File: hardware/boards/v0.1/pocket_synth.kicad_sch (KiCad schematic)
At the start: 7 parts

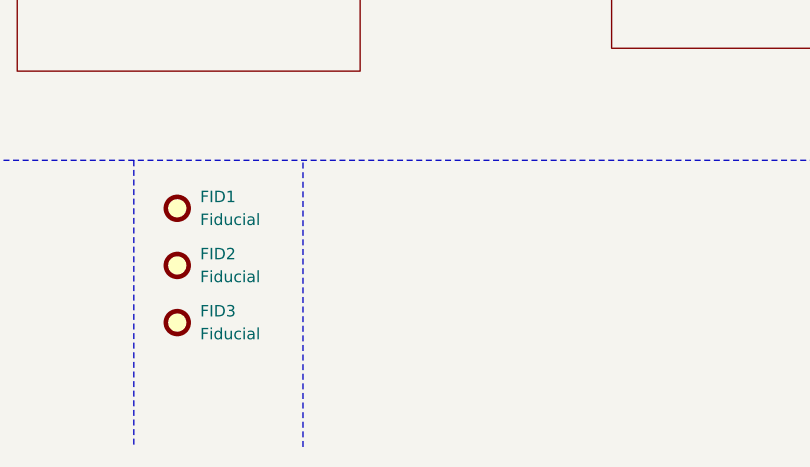
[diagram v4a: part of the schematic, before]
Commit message: feat: route thermalcouple, add top side fiducials
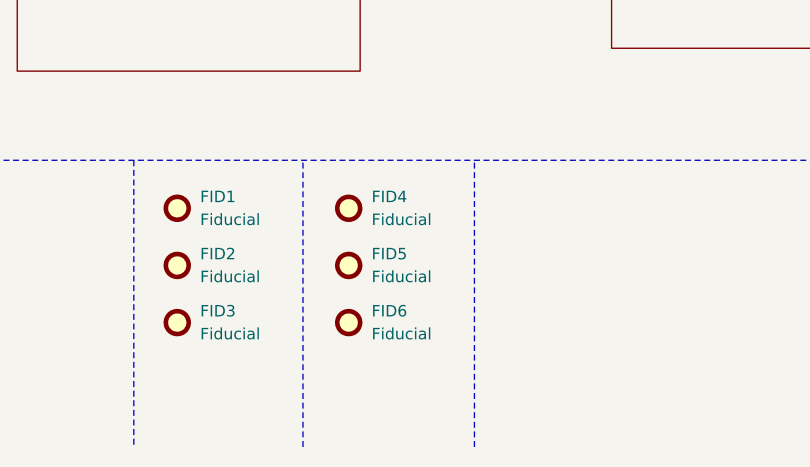
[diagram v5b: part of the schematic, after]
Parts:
- added FID4, FID5, FID6: Fiducial, Fiducial:Fiducial_0.5mm_Mask1.5mm, symbol Mechanical:Fiducial
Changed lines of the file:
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@@
+		)
+	)
+	(polyline
+		(pts
+			(xy 123.19 166.37) (xy 123.19 198.12)
+		)
+		(stroke
+			(width 0.127)
+			(type dash)
 		)
 	)
@@
 	)
 	(symbol
+		(lib_id "Mechanical:Fiducial")
+		(at 109.22 177.8 0)
+		(unit 1)
+		(exclude_from_sim no)
+		(in_bom no)
+		(on_board yes)
+		(dnp no)
+		(fields_autoplaced yes)
+		(property "Reference" "FID5"
+			(at 111.76 176.5299 0)
+			(effects
+				(font
+					(size 1.27 1.27)
+				)
+				(justify left)
+			)
+		)
+		(property "Value" "Fiducial"
+			(at 111.76 179.0699 0)
+			(effects
+				(font
+					(size 1.27 1.27)
+				)
+				(justify left)
+			)
+		)
+		(property "Footprint" "Fiducial:Fiducial_0.5mm_Mask1.5mm"
+			(at 109.22 177.8 0)
+			(effects
+				(font
+					(size 1.27 1.27)
+				)
+				(hide yes)
+			)
+		)
+		(property "Datasheet" "~"
+			(at 109.22 177.8 0)
+			(effects
+				(font
+					(size 1.27 1.27)
+				)
+				(hide yes)
+			)
+		)
+		(property "Description" "Fiducial Marker"
+			(at 109.22 177.8 0)
+			(effects
+				(font
+					(size 1.27 1.27)
+				)
+				(hide yes)
+			)
+		)
+		(instances
+			(project "pocket_synth"
+				(path "/485383b8-00f4-4405-b270-de249939cff4"
+					(reference "FID5")
+					(unit 1)
+				)
+			)
+		)
+	)
+	(symbol
 		(lib_id "Mechanical:MountingHole_Pad")
 		(at 48.26 182.88 0)
@@
 	(symbol
 		(lib_id "Mechanical:Fiducial")
+		(at 109.22 184.15 0)
+		(unit 1)
+		(exclude_from_sim no)
+		(in_bom no)
+		(on_board yes)
+		(dnp no)
+		(fields_autoplaced yes)
+		(property "Reference" "FID6"
+			(at 111.76 182.8799 0)
+			(effects
+				(font
+					(size 1.27 1.27)
+				)
+				(justify left)
+			)
+		)
+		(property "Value" "Fiducial"
+			(at 111.76 185.4199 0)
+			(effects
+				(font
+					(size 1.27 1.27)
+				)
+				(justify left)
+			)
+		)
+		(property "Footprint" "Fiducial:Fiducial_0.5mm_Mask1.5mm"
+			(at 109.22 184.15 0)
+			(effects
+				(font
+					(size 1.27 1.27)
+				)
+				(hide yes)
+			)
+		)
+		(property "Datasheet" "~"
+			(at 109.22 184.15 0)
+			(effects
+				(font
+					(size 1.27 1.27)
+				)
+				(hide yes)
+			)
+		)
+		(property "Description" "Fiducial Marker"
+			(at 109.22 184.15 0)
+			(effects
+				(font
+					(size 1.27 1.27)
+				)
+				(hide yes)
+			)
+		)
+		(instances
+			(project "pocket_synth"
+				(path "/485383b8-00f4-4405-b270-de249939cff4"
+					(reference "FID6")
+					(unit 1)
+				)
+			)
+		)
+	)
+	(symbol
+		(lib_id "Mechanical:Fiducial")
 		(at 90.17 184.15 0)
 		(unit 1)
@@
 					(unit 1)
 				)
+			)
+		)
+	)
+	(symbol
+		(lib_id "Mechanical:Fiducial")
+		(at 109.22 171.45 0)
+		(unit 1)
+		(exclude_from_sim no)
+		(in_bom no)
+		(on_board yes)
+		(dnp no)
+		(fields_autoplaced yes)
+		(property "Reference" "FID4"
+			(at 111.76 170.1799 0)
+			(effects
+				(font
+					(size 1.27 1.27)
+				)
+				(justify left)
+			)
+		)
+		(property "Value" "Fiducial"
+			(at 111.76 172.7199 0)
+			(effects
+				(font
+					(size 1.27 1.27)
+				)
+				(justify left)
+			)
+		)
+		(property "Footprint" "Fiducial:Fiducial_0.5mm_Mask1.5mm"
+			(at 109.22 171.45 0)
+			(effects
+				(font
+					(size 1.27 1.27)
+				)
+				(hide yes)
+			)
+		)
+		(property "Datasheet" "~"
+			(at 109.22 171.45 0)
+			(effects
+				(font
+					(size 1.27 1.27)
+				)
+				(hide yes)
+			)
+		)
+		(property "Description" "Fiducial Marker"
+			(at 109.22 171.45 0)
+			(effects
+				(font
+					(size 1.27 1.27)
+				)
+				(hide yes)
+			)
+		)
+		(instances
+			(project "pocket_synth"
+				(path "/485383b8-00f4-4405-b270-de249939cff4"
+					(reference "FID4")
+					(unit 1)
+				)

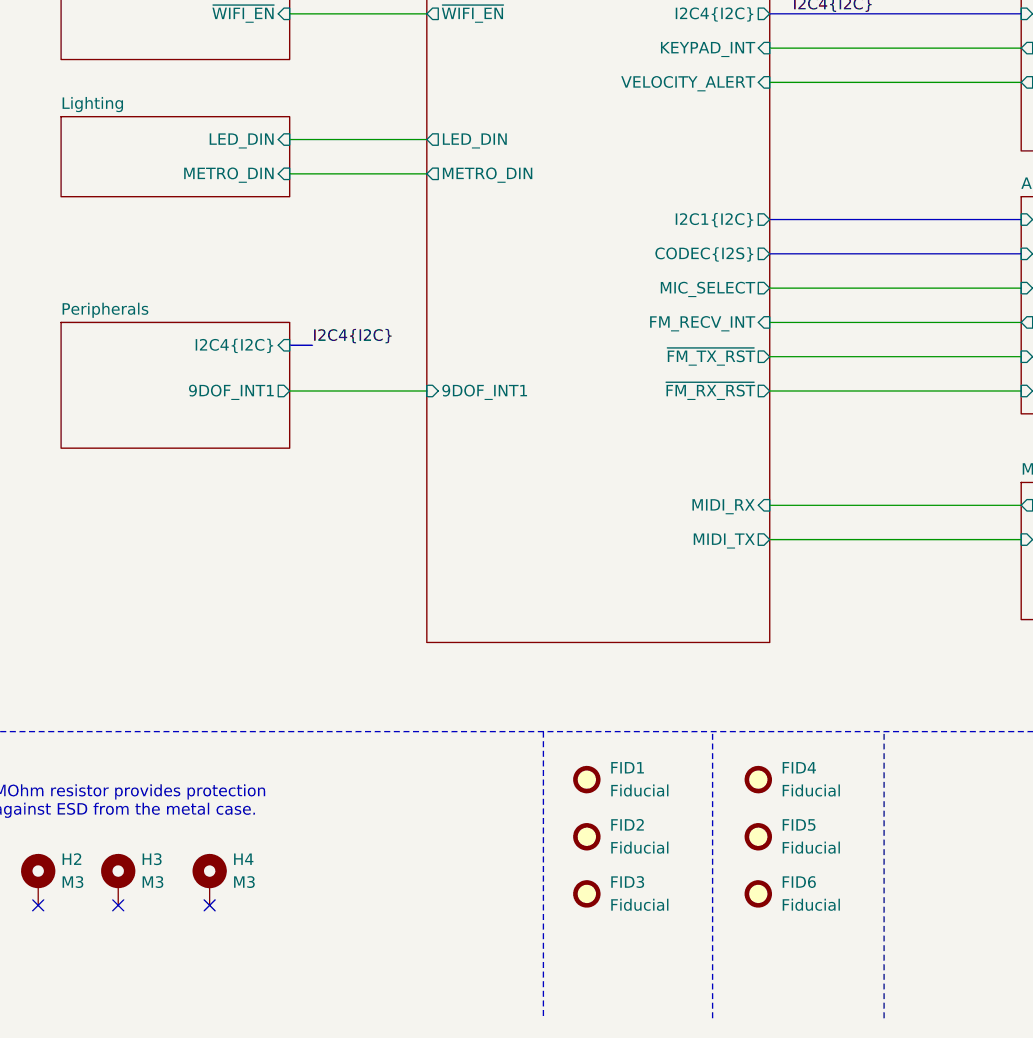
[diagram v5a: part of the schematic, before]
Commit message: feat: clean up routing, remove metronome light
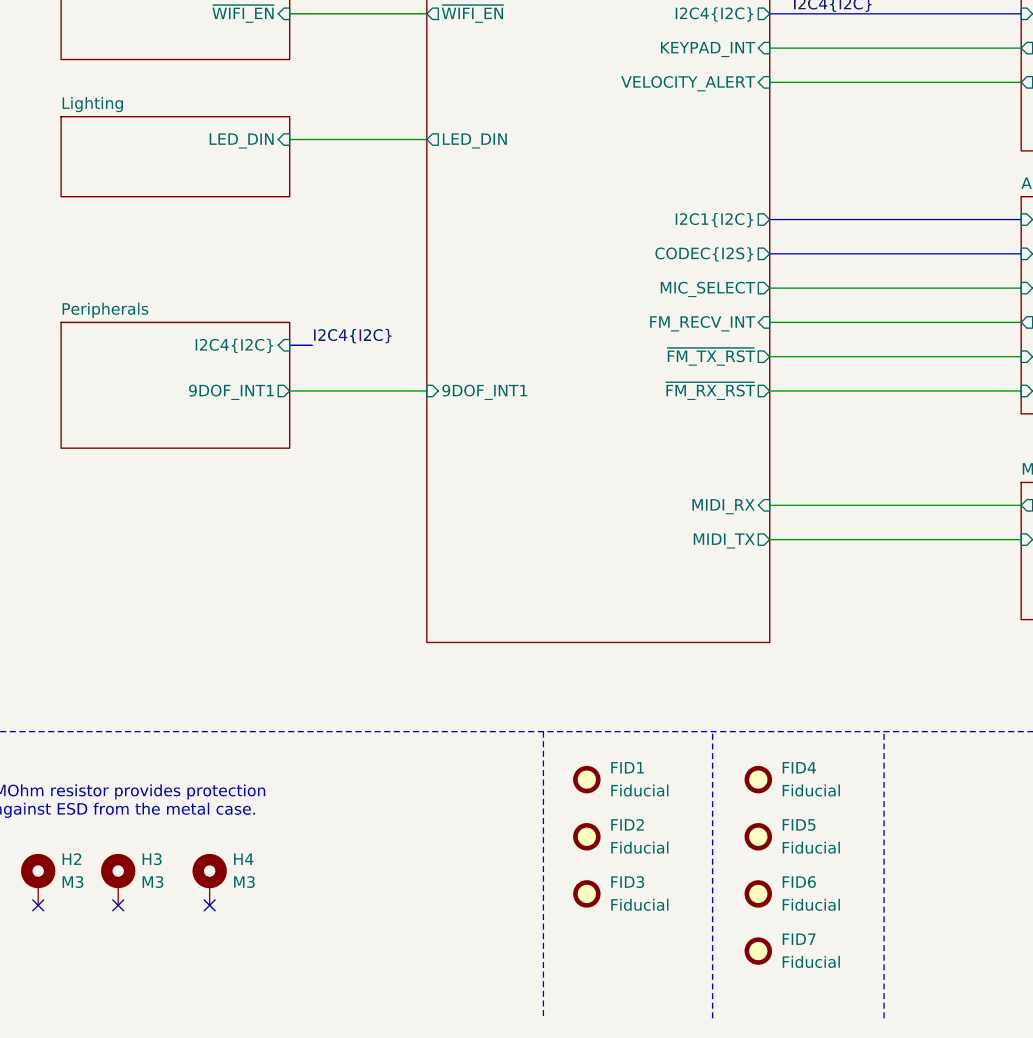
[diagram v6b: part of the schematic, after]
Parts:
- added FID7: Fiducial, Fiducial:Fiducial_0.5mm_Mask1.5mm, symbol Mechanical:Fiducial
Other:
- sheet Lighting ports: added none; removed METRO_DIN
- sheet MCU ports: added none; removed METRO_DIN
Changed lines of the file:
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@@
-	(wire
-		(pts
-			(xy 57.15 104.14) (xy 72.39 104.14)
-		)
-		(stroke
-			(width 0)
-			(type default)
-		)
-	)
 	(wire
 		(pts
@@
 	(symbol
 		(lib_id "Mechanical:Fiducial")
+		(at 109.22 190.5 0)
+		(unit 1)
+		(exclude_from_sim no)
+		(in_bom no)
+		(on_board yes)
+		(dnp no)
+		(fields_autoplaced yes)
+		(property "Reference" "FID7"
+			(at 111.76 189.2299 0)
+			(effects
+				(font
+					(size 1.27 1.27)
+				)
+				(justify left)
+			)
+		)
+		(property "Value" "Fiducial"
+			(at 111.76 191.7699 0)
+			(effects
+				(font
+					(size 1.27 1.27)
+				)
+				(justify left)
+			)
+		)
+		(property "Footprint" "Fiducial:Fiducial_0.5mm_Mask1.5mm"
+			(at 109.22 190.5 0)
+			(effects
+				(font
+					(size 1.27 1.27)
+				)
+				(hide yes)
+			)
+		)
+		(property "Datasheet" "~"
+			(at 109.22 190.5 0)
+			(effects
+				(font
+					(size 1.27 1.27)
+				)
+				(hide yes)
+			)
+		)
+		(property "Description" "Fiducial Marker"
+			(at 109.22 190.5 0)
+			(effects
+				(font
+					(size 1.27 1.27)
+				)
+				(hide yes)
+			)
+		)
+		(instances
+			(project "pocket_synth"
+				(path "/485383b8-00f4-4405-b270-de249939cff4"
+					(reference "FID7")
+					(unit 1)
+				)
+			)
+		)
+	)
+	(symbol
+		(lib_id "Mechanical:Fiducial")
 		(at 90.17 177.8 0)
 		(unit 1)
@@
 			)
 		)
-		(pin "METRO_DIN" output
-			(at 72.39 104.14 180)
-			(effects
-				(font
-					(size 1.27 1.27)
-				)
-				(justify left)
-			)
-		)
 		(pin "VELOCITY_ALERT" input
 			(at 110.49 93.98 0)
@@
 			(effects
 				(font
-					(size 1.27 1.27)
-				)
-				(justify right)
-			)
-		)
-		(pin "METRO_DIN" input
-			(at 57.15 104.14 0)
-			(effects
-				(font

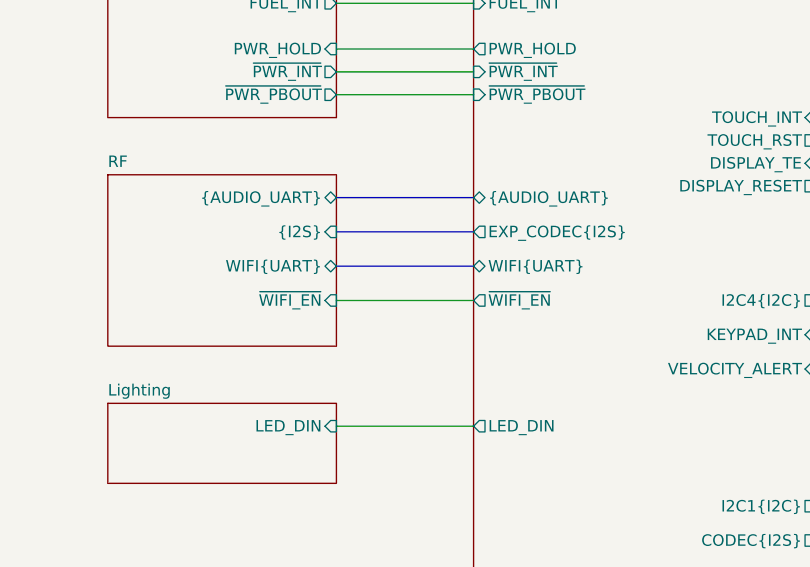
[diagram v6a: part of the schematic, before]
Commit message: feat: routing cleanup and start of BOM selection
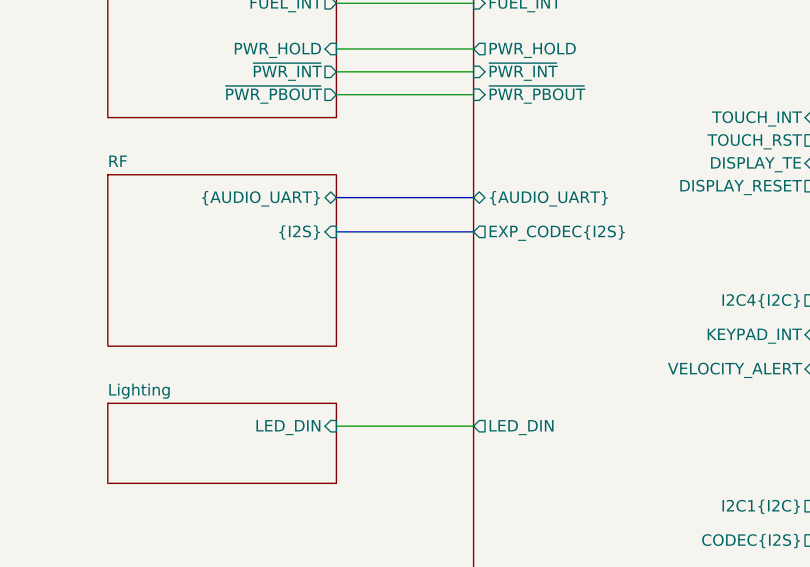
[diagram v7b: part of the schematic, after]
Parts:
- FID1, FID2, FID3, FID4, FID5, FID6, FID7: footprint Fiducial:Fiducial_0.5mm_Mask1.5mm -> PCM_kikit:Fiducial; now in the parts list
- H1, H2, H3, H4: now in the parts list
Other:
- sheet MCU ports: added none; removed WIFI{UART}, ~{WIFI_EN}
- sheet RF ports: added none; removed WIFI{UART}, ~{WIFI_EN}
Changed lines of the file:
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@@
-		)
-	)
-	(bus
-		(pts
-			(xy 57.15 82.55) (xy 72.39 82.55)
-		)
-		(stroke
-			(width 0)
-			(type default)
 		)
 	)
@@
 		(pts
 			(xy 110.49 86.36) (xy 138.43 86.36)
-		)
-		(stroke
-			(width 0)
-			(type default)
-		)
-	)
-	(wire
-		(pts
-			(xy 57.15 86.36) (xy 72.39 86.36)
 		)
 		(stroke
@@
 		(unit 1)
 		(exclude_from_sim no)
-		(in_bom no)
+		(in_bom yes)
 		(on_board yes)
 		(dnp no)
@@
 		(unit 1)
 		(exclude_from_sim no)
-		(in_bom no)
+		(in_bom yes)
 		(on_board yes)
 		(dnp no)
@@
 			)
 		)
-		(property "Footprint" "Fiducial:Fiducial_0.5mm_Mask1.5mm"
+		(property "Footprint" "PCM_kikit:Fiducial"
 			(at 109.22 177.8 0)
 			(effects
@@
 		(unit 1)
 		(exclude_from_sim no)
-		(in_bom no)
+		(in_bom yes)
 		(on_board yes)
 		(dnp no)
@@
 		(unit 1)
 		(exclude_from_sim no)
-		(in_bom no)
+		(in_bom yes)
 		(on_board yes)
 		(dnp no)
@@
 		(unit 1)
 		(exclude_from_sim no)
-		(in_bom no)
+		(in_bom yes)
 		(on_board yes)
 		(dnp no)
@@
 		(unit 1)
 		(exclude_from_sim no)
-		(in_bom no)
+		(in_bom yes)
 		(on_board yes)
 		(dnp no)
@@
 			)
 		)
-		(property "Footprint" "Fiducial:Fiducial_0.5mm_Mask1.5mm"
+		(property "Footprint" "PCM_kikit:Fiducial"
 			(at 90.17 171.45 0)
 			(effects
@@
 		(unit 1)
 		(exclude_from_sim no)
-		(in_bom no)
+		(in_bom yes)
 		(on_board yes)
 		(dnp no)
@@
 			)
 		)
-		(property "Footprint" "Fiducial:Fiducial_0.5mm_Mask1.5mm"
+		(property "Footprint" "PCM_kikit:Fiducial"
 			(at 109.22 184.15 0)
 			(effects
@@
 		(unit 1)
 		(exclude_from_sim no)
-		(in_bom no)
+		(in_bom yes)
 		(on_board yes)
 		(dnp no)
@@
 			)
 		)
-		(property "Footprint" "Fiducial:Fiducial_0.5mm_Mask1.5mm"
+		(property "Footprint" "PCM_kikit:Fiducial"
 			(at 90.17 184.15 0)
 			(effects
@@
 		(unit 1)
 		(exclude_from_sim no)
-		(in_bom no)
+		(in_bom yes)
 		(on_board yes)
 		(dnp no)
@@
 			)
 		)
-		(property "Footprint" "Fiducial:Fiducial_0.5mm_Mask1.5mm"
+		(property "Footprint" "PCM_kikit:Fiducial"
 			(at 109.22 171.45 0)
 			(effects
@@
 		(unit 1)
 		(exclude_from_sim no)
-		(in_bom no)
+		(in_bom yes)
 		(on_board yes)
 		(dnp no)
@@
 			)
 		)
-		(property "Footprint" "Fiducial:Fiducial_0.5mm_Mask1.5mm"
+		(property "Footprint" "PCM_kikit:Fiducial"
 			(at 109.22 190.5 0)
 			(effects
@@
 		(unit 1)
 		(exclude_from_sim no)
-		(in_bom no)
+		(in_bom yes)
 		(on_board yes)
 		(dnp no)
@@
 			)
 		)
-		(property "Footprint" "Fiducial:Fiducial_0.5mm_Mask1.5mm"
+		(property "Footprint" "PCM_kikit:Fiducial"
 			(at 90.17 177.8 0)
 			(effects
@@
 			)
 		)
-		(pin "WIFI{UART}" bidirectional
-			(at 72.39 82.55 180)
-			(effects
-				(font
-					(size 1.27 1.27)
-				)
-				(justify left)
-			)
-		)
 		(pin "I2C4{I2C}" output
 			(at 110.49 86.36 0)
@@
 		(pin "FUEL_INT" input
 			(at 72.39 53.34 180)
-			(effects
-				(font
-					(size 1.27 1.27)
-				)
-				(justify left)
-			)
-		)
-		(pin "~{WIFI_EN}" output
-			(at 72.39 86.36 180)
 			(effects
 				(font
@@
 			(effects
 				(font
-					(size 1.27 1.27)
-				)
-				(justify right)
-			)
-		)
-		(pin "WIFI{UART}" bidirectional
-			(at 57.15 82.55 0)
-			(effects
-				(font
-					(size 1.27 1.27)
-				)
-				(justify right)
-			)
-		)
-		(pin "~{WIFI_EN}" input
-			(at 57.15 86.36 0)
-			(effects
-				(font
